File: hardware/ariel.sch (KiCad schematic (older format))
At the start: 20 parts, among them SW1 SW_Push, U1 WeMos_Battery_Shield, U2 WeMos_D1_mini, U3 74HC595, U4 Si7021_breakout

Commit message: Tweak WeMos battery shield footprint
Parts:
- U1: footprint WeMos:D1_mini_board -> WeMos:Battery_shield
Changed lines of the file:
@@
 F 0 "U1" H 2200 2550 60  0000 C CNN
 F 1 "WeMos_Battery_Shield" H 2300 1400 60  0000 C CNN
-F 2 "WeMos:D1_mini_board" H 2200 1300 60  0001 C CNN
+F 2 "WeMos:Battery_shield" H 2200 1300 60  0001 C CNN
 F 3 "http://www.wemos.cc/Products/d1_mini.html" H 1800 2794 60  0001 C CNN
 	1    1800 2000

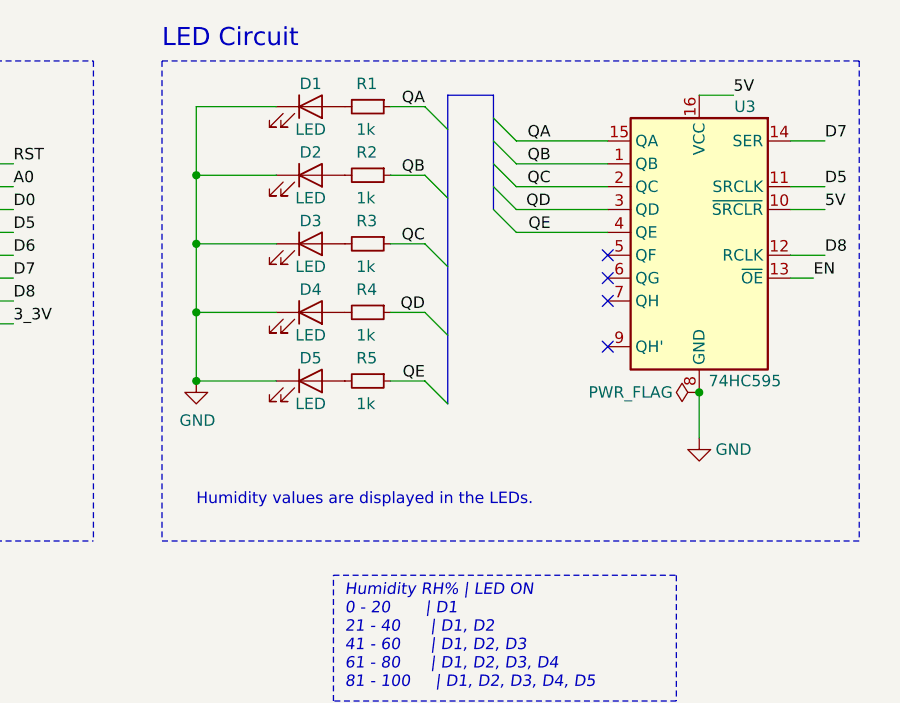
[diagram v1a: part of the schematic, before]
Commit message: Layout tracks and fix footprint
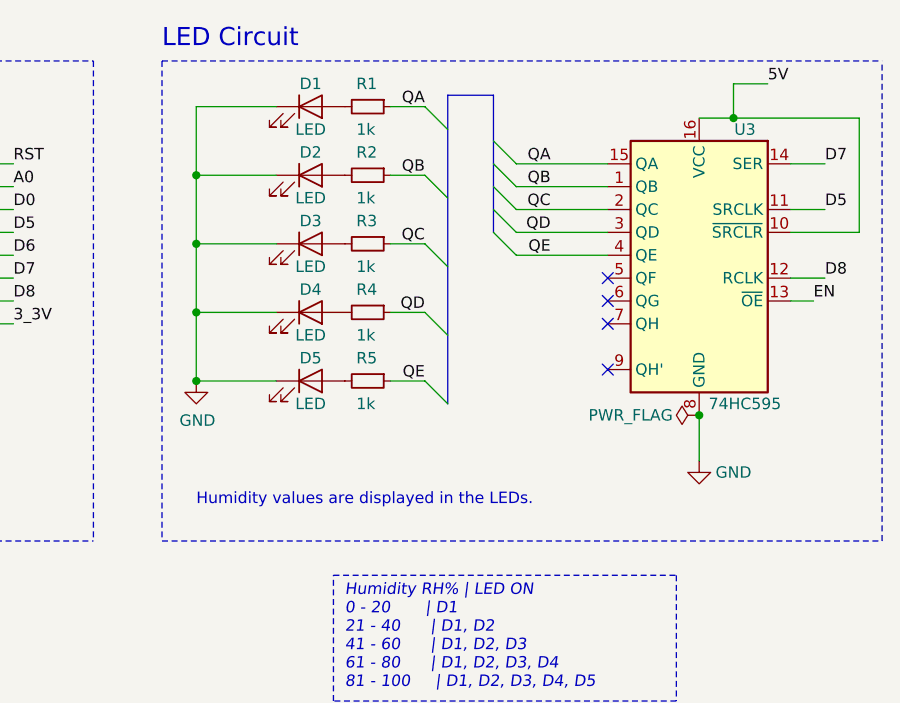
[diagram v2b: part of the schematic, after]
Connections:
- wire segments 64 -> 68
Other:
- moved on the sheet: U3
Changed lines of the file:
@@
 L 74xx:74HC595 U3
 U 1 1 5C77296E
-P 8650 1650
-F 0 "U3" H 8450 2200 50  0000 C CNN
-F 1 "74HC595" H 8450 1000 50  0000 C CNN
-F 2 "Package_SO:SOIC-16_3.9x9.9mm_P1.27mm" H 8650 1650 50  0001 C CNN
-F 3 "http://www.ti.com/lit/ds/symlink/sn74hc595.pdf" H 8650 1650 50  0001 C CNN
-	1    8650 1650
+P 8650 1750
+F 0 "U3" H 8450 2300 50  0000 C CNN
+F 1 "74HC595" H 8450 1100 50  0000 C CNN
+F 2 "Package_SO:SOIC-16_3.9x9.9mm_P1.27mm" H 8650 1750 50  0001 C CNN
+F 3 "http://www.ti.com/lit/ds/symlink/sn74hc595.pdf" H 8650 1750 50  0001 C CNN
+	1    8650 1750
 	-1   0    0    -1
 $EndComp
@@
 L power:GND #PWR07
 U 1 1 5C8625CA
-P 8650 2550
-F 0 "#PWR07" H 8650 2300 50  0001 C CNN
-F 1 "GND" H 8800 2500 50  0000 C CNN
-F 2 "" H 8650 2550 50  0001 C CNN
-F 3 "" H 8650 2550 50  0001 C CNN
-	1    8650 2550
+P 8650 2650
+F 0 "#PWR07" H 8650 2400 50  0001 C CNN
+F 1 "GND" H 8800 2600 50  0000 C CNN
+F 2 "" H 8650 2650 50  0001 C CNN
+F 3 "" H 8650 2650 50  0001 C CNN
+	1    8650 2650
 	1    0    0    -1
 $EndComp
@@
 	1    0    0    -1
 $EndComp
-NoConn ~ 8250 1750
 NoConn ~ 8250 1850
 NoConn ~ 8250 1950
-NoConn ~ 8250 2150
+NoConn ~ 8250 2050
+NoConn ~ 8250 2250
 $Comp
 L power:GND #PWR03
@@
 Text Label 5650 2050 0    50   ~ 0
 3_3V
-Text Label 8800 1050 0    50   ~ 0
-5V
 Text Label 5650 1950 0    50   ~ 0
 D8
-Text Label 9200 1750 0    50   ~ 0
+Text Label 9200 1850 0    50   ~ 0
 D8
-Text Label 9200 1250 0    50   ~ 0
+Text Label 9200 1350 0    50   ~ 0
 D7
 Text Label 5650 1850 0    50   ~ 0
 D7
-Text Label 9200 1450 0    50   ~ 0
+Text Label 9200 1550 0    50   ~ 0
 D5
 Text Label 5650 1650 0    50   ~ 0
@@
 	6450 1700 6800 1700
 Wire Wire Line
-	9050 1250 9200 1250
-Wire Wire Line
-	9050 1450 9200 1450
-Wire Wire Line
-	9050 1750 9200 1750
-Wire Wire Line
-	8650 1050 8800 1050
+	9050 1350 9200 1350
+Wire Wire Line
+	9050 1550 9200 1550
+Wire Wire Line
+	9050 1850 9200 1850
 $Comp
 L power:PWR_FLAG #FLG02
 U 1 1 5C8B6759
-P 8650 2350
-F 0 "#FLG02" H 8650 2425 50  0001 C CNN
-F 1 "PWR_FLAG" V 8650 2650 50  0000 C CNN
-F 2 "" H 8650 2350 50  0001 C CNN
-F 3 "~" H 8650 2350 50  0001 C CNN
-	1    8650 2350
+P 8650 2450
+F 0 "#FLG02" H 8650 2525 50  0001 C CNN
+F 1 "PWR_FLAG" V 8650 2750 50  0000 C CNN
+F 2 "" H 8650 2450 50  0001 C CNN
+F 3 "~" H 8650 2450 50  0001 C CNN
+	1    8650 2450
 	0    -1   -1   0
 $EndComp
 Wire Wire Line
 	7300 1100 7450 1100
-Text Label 8000 1250 2    50   ~ 0
+Text Label 8000 1350 2    50   ~ 0
 QA
 Text Label 7450 1100 2    50   ~ 0
 QA
 Entry Wire Line
-	7750 1150 7850 1250
-Entry Wire Line
 	7750 1250 7850 1350
 Entry Wire Line
@@
 Entry Wire Line
 	7750 1550 7850 1650
-Text Label 8000 1350 2    50   ~ 0
+Entry Wire Line
+	7750 1650 7850 1750
+Text Label 8000 1450 2    50   ~ 0
 QB
-Text Label 8000 1450 2    50   ~ 0
+Text Label 8000 1550 2    50   ~ 0
 QC
-Text Label 8000 1550 2    50   ~ 0
+Text Label 8000 1650 2    50   ~ 0
 QD
-Text Label 8000 1650 2    50   ~ 0
+Text Label 8000 1750 2    50   ~ 0
 QE
 Wire Wire Line
@@
 Text Notes 6450 2850 0    50   ~ 0
 Humidity values are displayed in the LEDs.
-Wire Notes Line
-	6300 900  9350 900
-Wire Wire Line
-	7850 1250 8250 1250
 Wire Wire Line
 	7850 1350 8250 1350
@@
 Wire Wire Line
 	7850 1650 8250 1650
+Wire Wire Line
+	7850 1750 8250 1750
 NoConn ~ 1100 1700
 NoConn ~ 1100 1800
@@
 5V
 Wire Wire Line
-	9050 1850 9150 1850
-Connection ~ 8650 2350
-Wire Notes Line
-	6300 3000 9350 3000
+	9050 1950 9150 1950
+Connection ~ 8650 2450
 Wire Notes Line
 	6300 900  6300 3000
-Wire Notes Line
-	9350 900  9350 3000
-Wire Wire Line
-	9050 1550 9200 1550
-Text Label 9200 1550 0    50   ~ 0
-5V
 Wire Wire Line
 	4100 2000 3950 2000
@@
 EN
 Wire Wire Line
-	8650 2350 8650 2550
-Text Label 9150 1850 0    50   ~ 0
+	8650 2450 8650 2650
+Text Label 9150 1950 0    50   ~ 0
 EN
 $Comp
@@
 Wire Notes Line
 	900  3350 3200 3350
+Text Label 8950 1000 0    50   ~ 0
+5V
+Wire Wire Line
+	9350 1150 9350 1650
+Wire Wire Line
+	8650 1150 8800 1150
+Wire Wire Line
+	9050 1650 9350 1650
+Wire Notes Line
+	9450 3000 9450 900
+Wire Notes Line
+	6300 900  9450 900
+Wire Notes Line
+	6300 3000 9450 3000
+Wire Wire Line
+	8800 1150 8800 1000
+Connection ~ 8800 1150
+Wire Wire Line
+	8800 1150 9350 1150
+Wire Wire Line
+	8800 1000 8950 1000
 Wire Bus Line
 	7550 1050 7550 2400
 Wire Bus Line
-	7750 1050 7750 1550
+	7750 1050 7750 1650
 $EndSCHEMATC
